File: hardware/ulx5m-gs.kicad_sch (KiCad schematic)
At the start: 4 parts

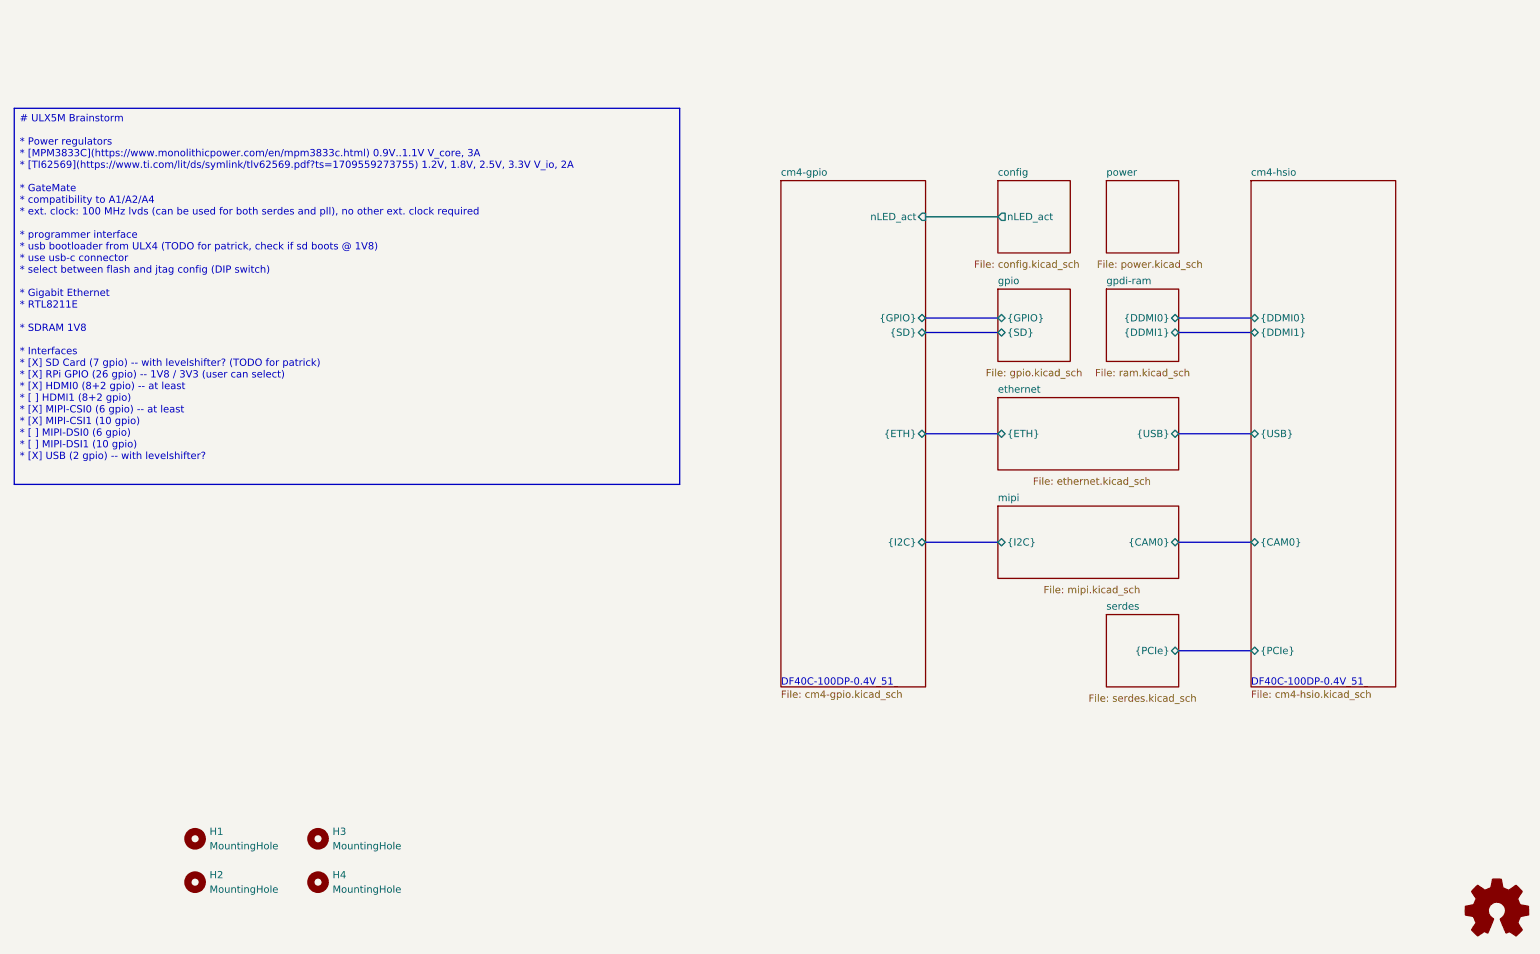
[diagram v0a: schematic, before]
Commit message: Adding USB connector and level converter
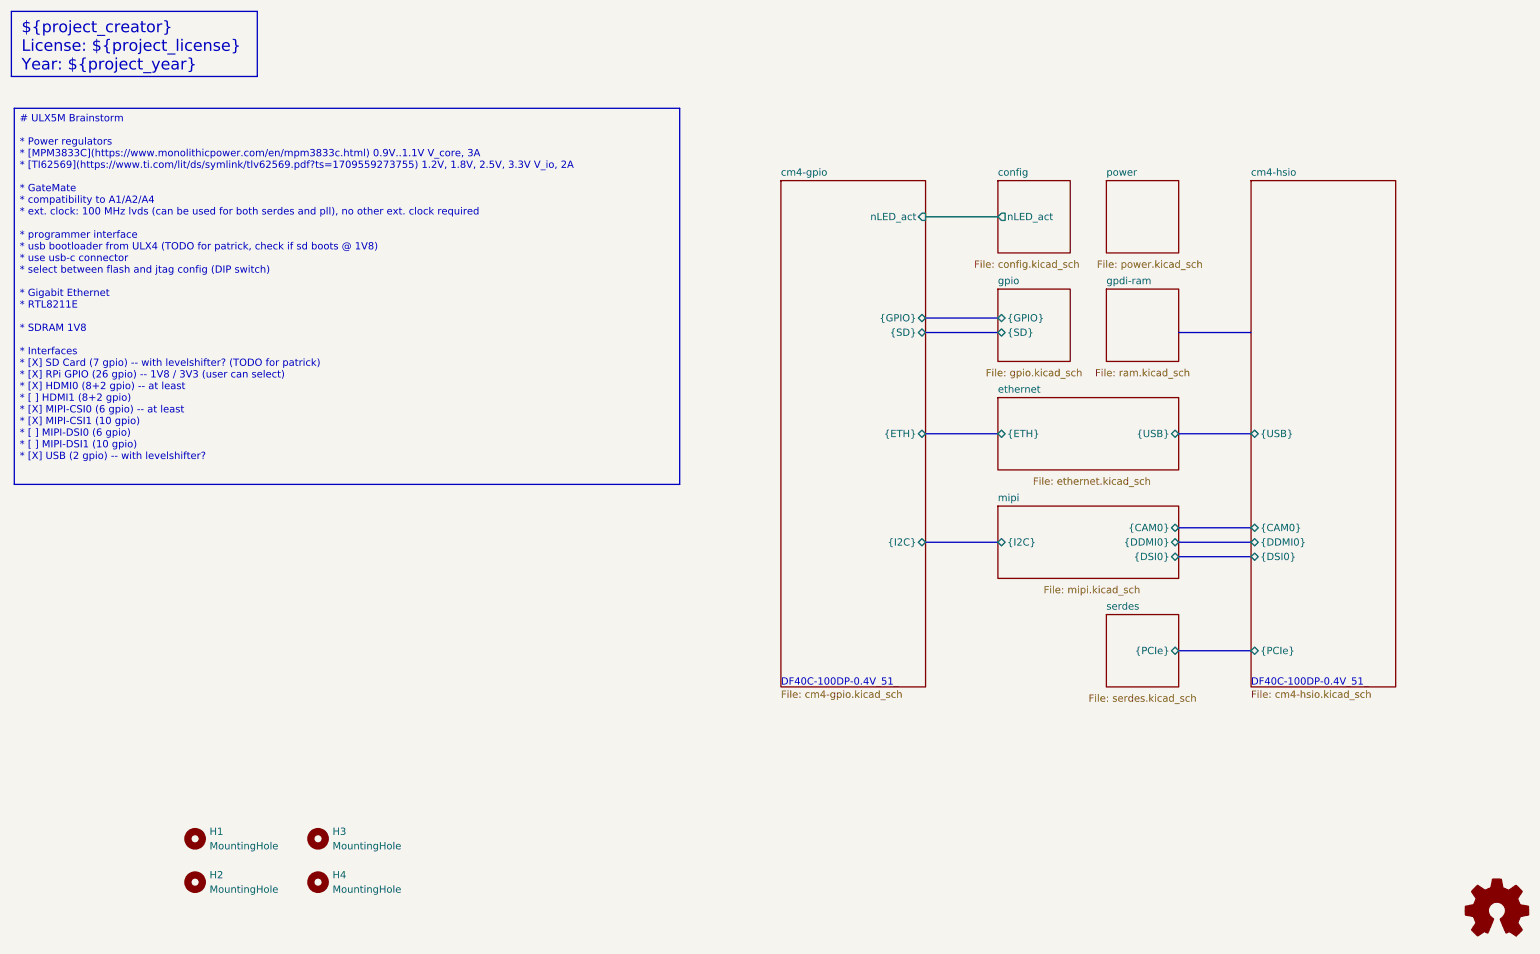
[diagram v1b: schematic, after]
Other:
- sheet cm4-hsio ports: added {DSI0}; removed {DDMI1}
- sheet gpdi-ram ports: added none; removed {DDMI0}, {DDMI1}
- sheet mipi ports: added {DDMI0}, {DSI0}; removed none
- note added: "${project_creator} License: ${project_license} Year: ${project_year}"
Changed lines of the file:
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@@
 		(date "2025-04-01")
+	)
+	(rectangle
+		(start 16.002 16.002)
+		(end 59.182 27.432)
+		(stroke
+			(width 0)
+			(type solid)
+		)
+		(fill
+			(type color)
+			(color 58 146 255 1)
+		)
 	)
 	(text "DF40C-100DP-0.4V_51_"
@@
 		)
 	)
+	(text "${project_creator}\nLicense: ${project_license}\nYear: ${project_year}"
+		(exclude_from_sim no)
+		(at 17.78 17.78 0)
+		(effects
+			(font
+				(size 2.032 2.032)
+			)
+			(justify left top)
+		)
+	)
 	(text_box "# ULX5M Brainstorm\n\n* Power regulators\n  * [MPM3833C](https://www.monolithicpower.com/en/mpm3833c.html) 0.9V..1.1V V_core, 3A\n  * [TI62569](https://www.ti.com/lit/ds/symlink/tlv62569.pdf?ts=1709559273755) 1.2V, 1.8V, 2.5V, 3.3V V_io, 2A\n\n* GateMate\n  * compatibility to A1/A2/A4\n  * ext. clock: 100 MHz lvds (can be used for both serdes and pll), no other ext. clock required\n\n* programmer interface\n  * usb bootloader from ULX4 (TODO for patrick, check if sd boots @ 1V8)\n  * use usb-c connector\n  * select between flash and jtag config (DIP switch)\n\n* Gigabit Ethernet\n  * RTL8211E\n\n* SDRAM 1V8\n\n* Interfaces\n  * [X] SD Card (7 gpio) -- with levelshifter? (TODO for patrick)\n  * [X] RPi GPIO (26 gpio) -- 1V8 / 3V3 (user can select)\n  * [X] HDMI0 (8+2 gpio) -- at least\n  * [ ] HDMI1 (8+2 gpio)\n  * [X] MIPI-CSI0 (6 gpio) -- at least\n  * [X] MIPI-CSI1 (10 gpio)\n  * [ ] MIPI-DSI0 (6 gpio)\n  * [ ] MIPI-DSI1 (10 gpio)\n  * [X] USB (2 gpio) -- with levelshifter?\n\n"
 		(exclude_from_sim no)
@@
 	(bus
 		(pts
-			(xy 220.98 69.85) (xy 233.68 69.85)
+			(xy 220.98 106.68) (xy 233.68 106.68)
 		)
 		(stroke
@@
 		(pts
 			(xy 176.53 69.85) (xy 189.23 69.85)
+		)
+		(stroke
+			(width 0)
+			(type default)
+		)
+	)
+	(bus
+		(pts
+			(xy 220.98 111.76) (xy 233.68 111.76)
 		)
 		(stroke
@@
 		)
 		(pin "{CAM0}" bidirectional
+			(at 220.98 106.68 0)
+			(effects
+				(font
+					(size 1.27 1.27)
+				)
+				(justify right)
+			)
+		)
+		(pin "{DDMI0}" bidirectional
 			(at 220.98 109.22 0)
+			(effects
+				(font
+					(size 1.27 1.27)
+				)
+				(justify right)
+			)
+		)
+		(pin "{DSI0}" bidirectional
+			(at 220.98 111.76 0)
 			(effects
 				(font
@@
 		)
 		(pin "{DDMI0}" bidirectional
-			(at 233.68 69.85 180)
+			(at 233.68 109.22 180)
 			(effects
 				(font
@@
 		)
 		(pin "{CAM0}" bidirectional
-			(at 233.68 109.22 180)
+			(at 233.68 106.68 180)
 			(effects
 				(font
@@
 			)
 		)
-		(pin "{DDMI1}" bidirectional
-			(at 233.68 72.39 180)
+		(pin "{DSI0}" bidirectional
+			(at 233.68 111.76 180)
 			(effects
 				(font
@@
 			)
 		)
-		(pin "{DDMI0}" bidirectional
-			(at 220.98 69.85 0)
-			(effects
-				(font
-					(size 1.27 1.27)
-				)
-				(justify right)
-			)
-		)
-		(pin "{DDMI1}" bidirectional
-			(at 220.98 72.39 0)
-			(effects
-				(font
-					(size 1.27 1.27)
-				)
-				(justify right)
-			)
-		)

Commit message: Routing diff clock
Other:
- company: (none) -> ${project_creator}
- title: (none) -> ${project_name}
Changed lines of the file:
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@@
 	(paper "A4")
 	(title_block
-		(date "2025-04-01")
+		(title "${project_name}")
+		(date "2025-06-24")
+		(rev "${project_version}")
+		(company "${project_creator}")
+		(comment 1 "${project_license}")
 	)
 	(rectangle

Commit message: Updat to CM5
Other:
- sheet cm4-gpio ports: added EEPROM_nWP, ETH_SYNC_O, FAN_PWM, FAN_TACHO, GPIO_VREF, ID_SC, ID_SD, LED_nPWR, PWR_BTN, USB_CC1, USB_CC2, VBAT, nRpiBOOT; removed none
- sheet cm4-hsio ports: added {DDMI1}, {MIPI0}, {MIPI1}, {USB3_0}; removed {CAM0}, {DSI0}
- sheet ethernet ports: added ID_SC, ID_SD, USB_CC1, USB_CC2, {DDMI1}, {I2C}; removed none
- sheet mipi ports: added {MIPI0}, {MIPI1}; removed {CAM0}, {DSI0}, {I2C}

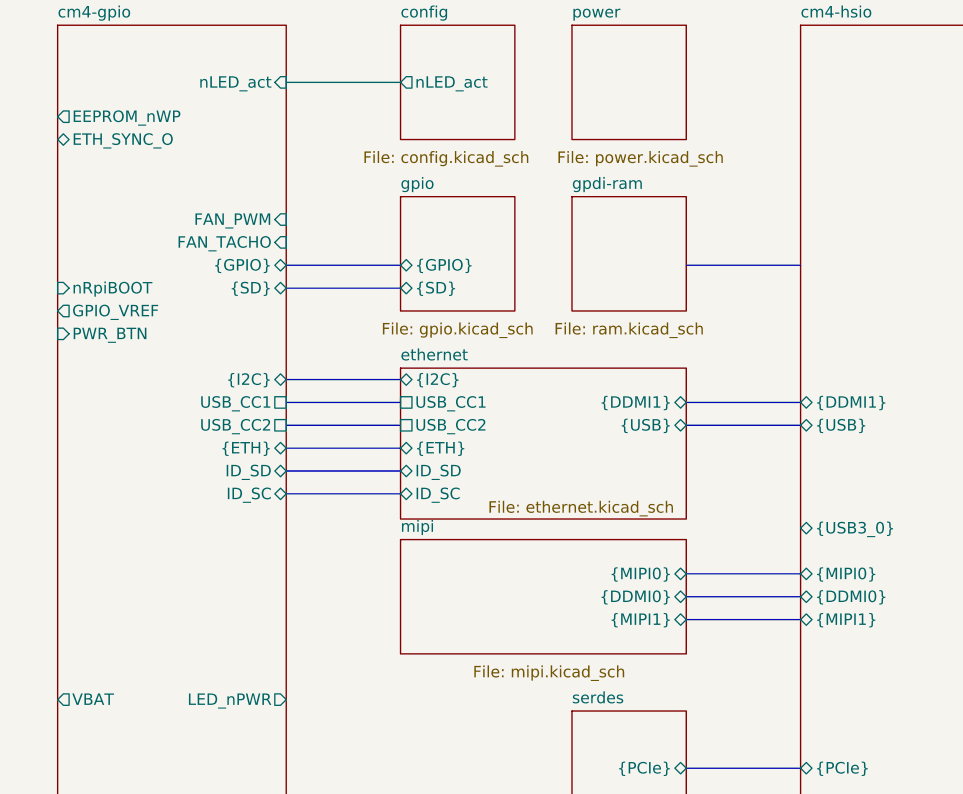
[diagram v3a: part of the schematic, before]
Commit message: Routing GPDI
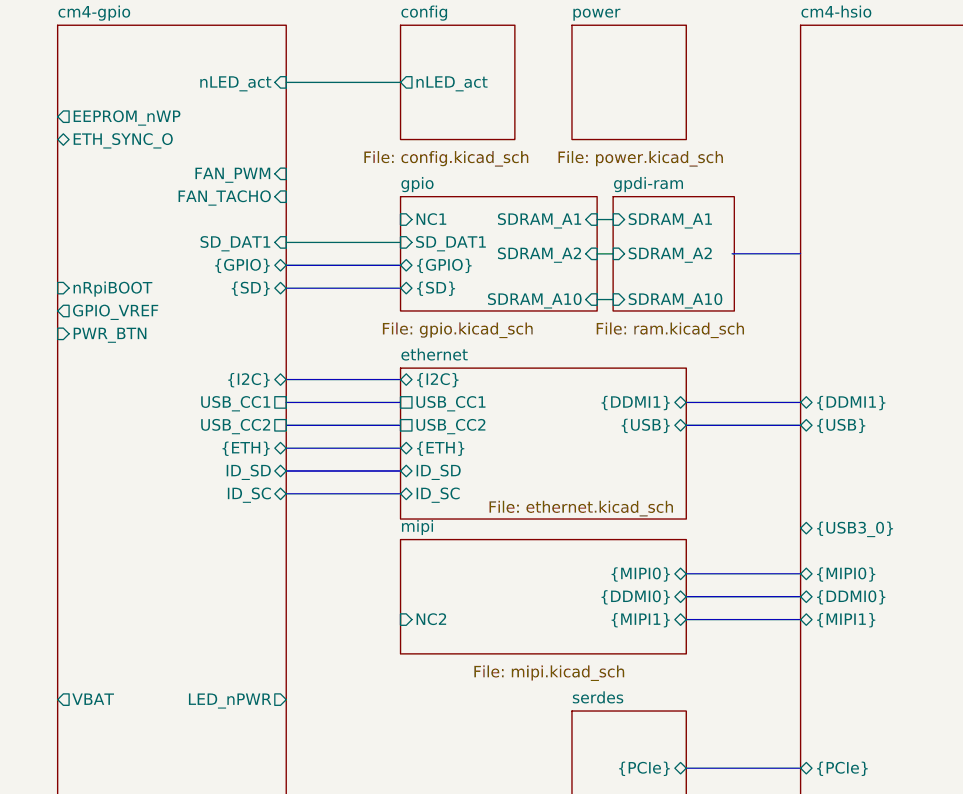
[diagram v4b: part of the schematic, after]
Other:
- sheet cm4-gpio ports: added SD_DAT1; removed none
- sheet gpdi-ram ports: added SDRAM_A1, SDRAM_A10, SDRAM_A2; removed none
- sheet gpio ports: added NC1, SDRAM_A1, SDRAM_A10, SDRAM_A2, SD_DAT1; removed none
- sheet mipi ports: added NC2; removed none
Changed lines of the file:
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@@
+		)
+	)
+	(wire
+		(pts
+			(xy 176.53 69.85) (xy 189.23 69.85)
+		)
+		(stroke
+			(width 0)
+			(type default)
 		)
 	)
@@
 		)
 	)
+	(wire
+		(pts
+			(xy 211.074 67.31) (xy 212.852 67.31)
+		)
+		(stroke
+			(width 0)
+			(type default)
+		)
+	)
 	(bus
 		(pts
@@
 		)
 	)
+	(wire
+		(pts
+			(xy 211.074 76.2) (xy 212.852 76.2)
+		)
+		(stroke
+			(width 0)
+			(type default)
+		)
+	)
 	(bus
 		(pts
@@
 		)
 	)
+	(wire
+		(pts
+			(xy 211.074 71.12) (xy 212.852 71.12)
+		)
+		(stroke
+			(width 0)
+			(type default)
+		)
+	)
 	(bus
 		(pts
@@
 		)
 	)
+	(bus
+		(pts
+			(xy 226.06 71.12) (xy 233.68 71.12)
+		)
+		(stroke
+			(width 0)
+			(type default)
+		)
+	)
 	(wire
 		(pts
 			(xy 176.53 52.07) (xy 189.23 52.07)
-		)
-		(stroke
-			(width 0)
-			(type default)
-		)
-	)
-	(bus
-		(pts
-			(xy 220.98 72.39) (xy 233.68 72.39)
 		)
 		(stroke
@@
 		)
 		(pin "FAN_PWM" input
-			(at 176.53 67.31 0)
+			(at 176.53 62.23 0)
 			(effects
 				(font
@@
 		)
 		(pin "FAN_TACHO" input
-			(at 176.53 69.85 0)
+			(at 176.53 64.77 0)
 			(effects
 				(font
@@
 				)
 				(justify left)
+			)
+		)
+		(pin "SD_DAT1" input
+			(at 176.53 69.85 0)
+			(effects
+				(font
+					(size 1.27 1.27)
+				)
+				(justify right)
 			)
 		)
@@
 	(sheet
 		(at 189.23 64.77)
-		(size 12.7 12.7)
+		(size 21.844 12.7)
 		(exclude_from_sim no)
 		(in_bom yes)
@@
 		(pin "{SD}" bidirectional
 			(at 189.23 74.93 180)
+			(effects
+				(font
+					(size 1.27 1.27)
+				)
+				(justify left)
+			)
+		)
+		(pin "SDRAM_A1" input
+			(at 211.074 67.31 0)
+			(effects
+				(font
+					(size 1.27 1.27)
+				)
+				(justify right)
+			)
+		)
+		(pin "SDRAM_A2" input
+			(at 211.074 71.12 0)
+			(effects
+				(font
+					(size 1.27 1.27)
+				)
+				(justify right)
+			)
+		)
+		(pin "SDRAM_A10" input
+			(at 211.074 76.2 0)
+			(effects
+				(font
+					(size 1.27 1.27)
+				)
+				(justify right)
+			)
+		)
+		(pin "SD_DAT1" input
+			(at 189.23 69.85 180)
+			(effects
+				(font
+					(size 1.27 1.27)
+				)
+				(justify left)
+			)
+		)
+		(pin "NC1" input
+			(at 189.23 67.31 180)
 			(effects
 				(font
@@
 			)
 		)
+		(pin "NC2" input
+			(at 189.23 111.76 180)
+			(effects
+				(font
+					(size 1.27 1.27)
+				)
+				(justify left)
+			)
+		)
 		(instances
 			(project "ulx5m-gs"
@@
 	)
 	(sheet
-		(at 208.28 64.77)
-		(size 12.7 12.7)
+		(at 212.852 64.77)
+		(size 13.462 12.7)
 		(exclude_from_sim no)
 		(in_bom yes)
@@
 		)
 		(property "Sheetname" "gpdi-ram"
-			(at 208.28 64.0584 0)
+			(at 212.852 64.0584 0)
 			(effects
 				(font
@@
 		)
 		(property "Sheetfile" "ram.kicad_sch"
-			(at 214.63 78.74 0)
+			(at 219.202 78.74 0)
 			(effects
 				(font
@@
 			)
 		)
+		(pin "SDRAM_A1" input
+			(at 212.852 67.31 180)
+			(effects
+				(font
+					(size 1.27 1.27)
+				)
+				(justify left)
+			)
+		)
+		(pin "SDRAM_A2" input
+			(at 212.852 71.12 180)
+			(effects
+				(font
+					(size 1.27 1.27)
+				)
+				(justify left)
+			)
+		)
+		(pin "SDRAM_A10" input
+			(at 212.852 76.2 180)
+			(effects
+				(font
+					(size 1.27 1.27)
+				)
+				(justify left)
+			)
+		)

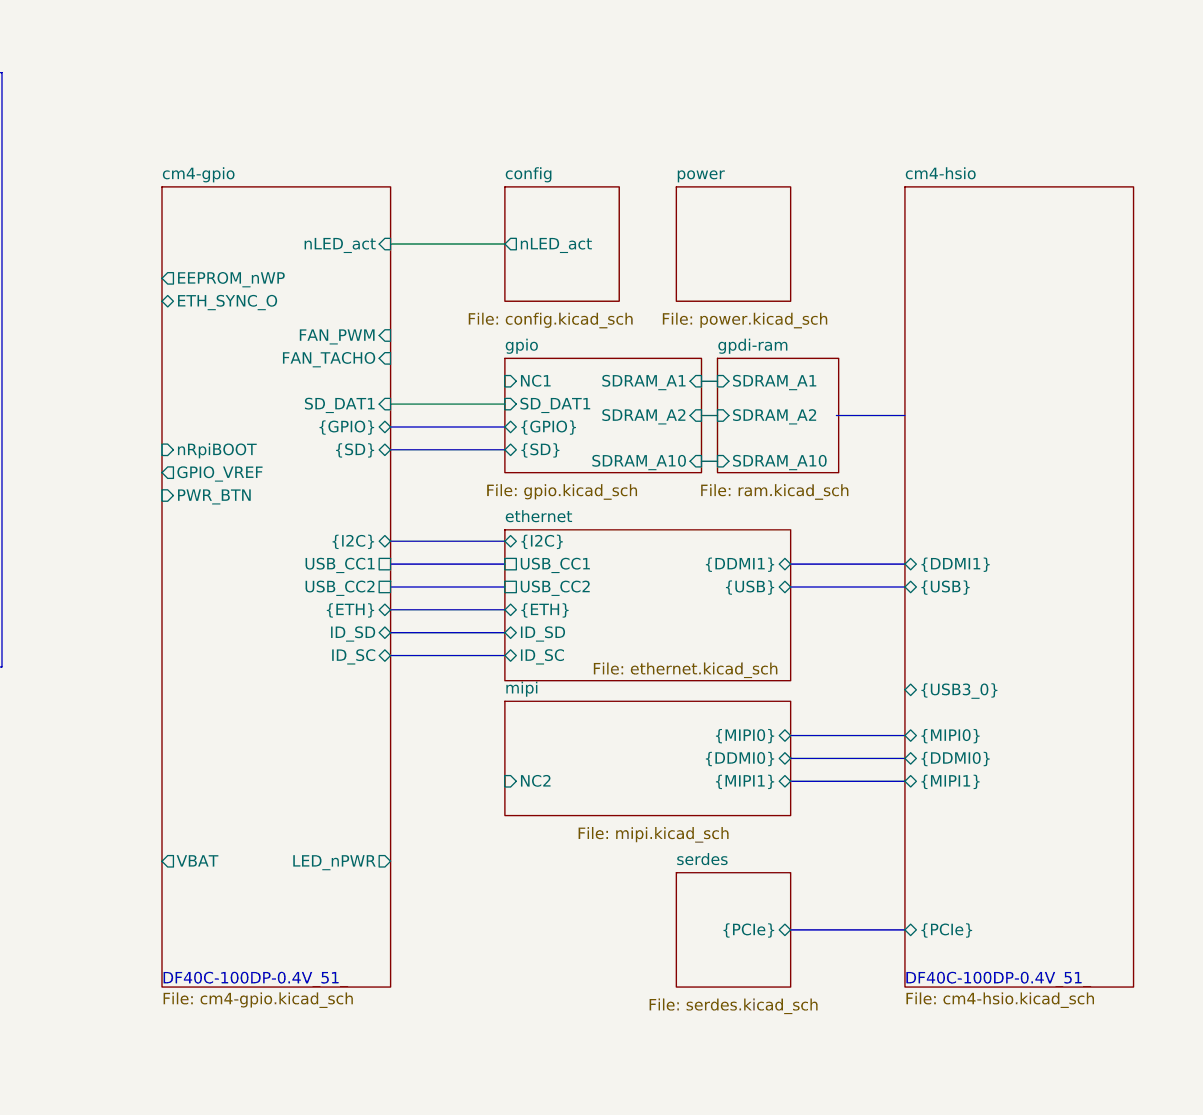
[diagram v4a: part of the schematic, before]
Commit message: Clearing ERC errors/warnings
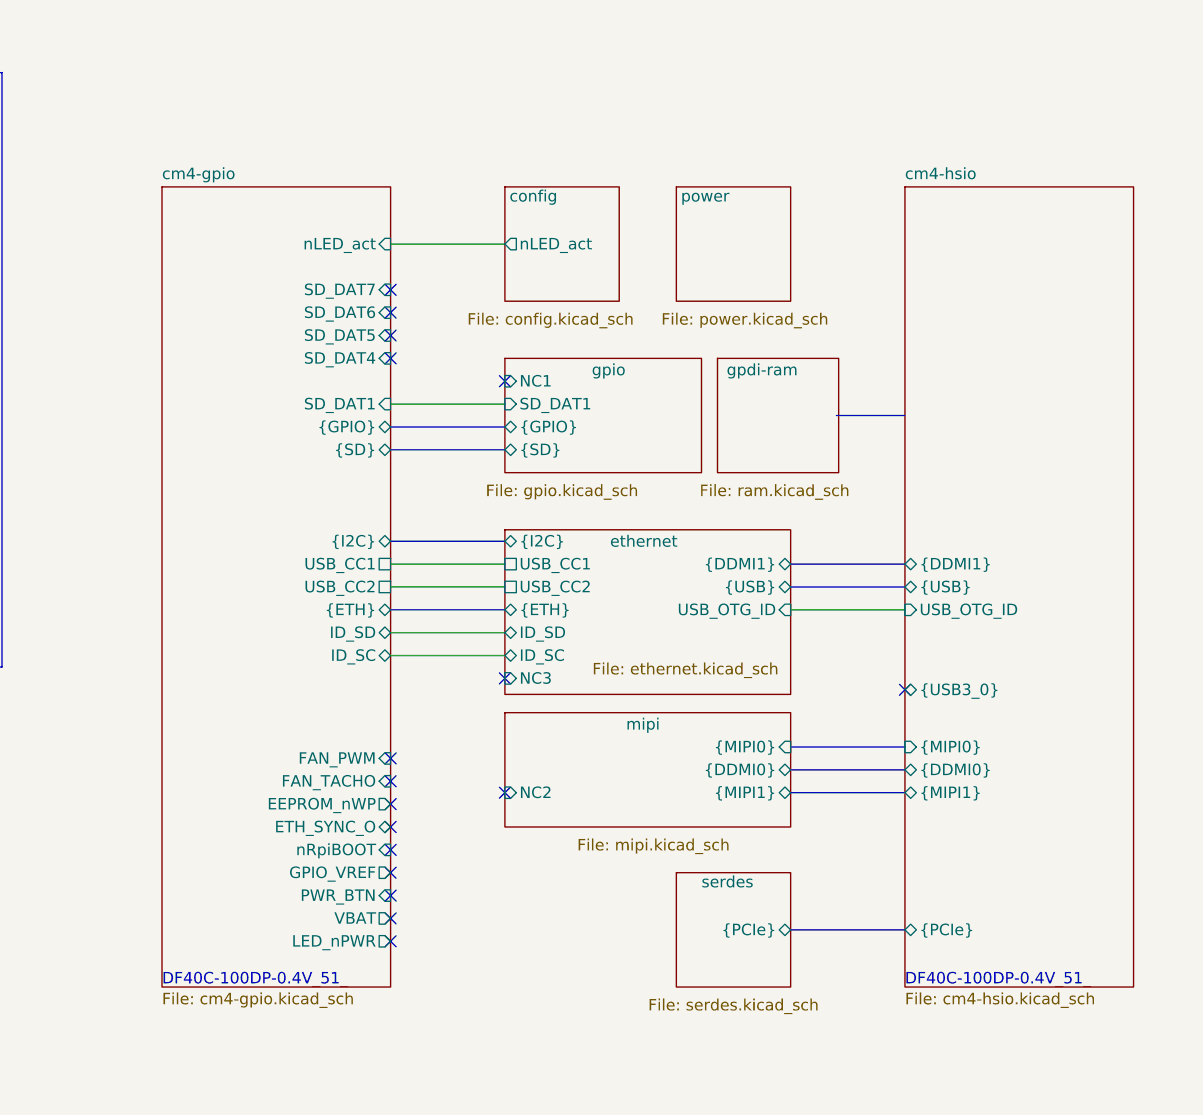
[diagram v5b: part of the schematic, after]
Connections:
- no-connect marks 0 -> 17
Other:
- sheet cm4-gpio ports: added SD_DAT4, SD_DAT5, SD_DAT6, SD_DAT7; removed none
- sheet cm4-hsio ports: added USB_OTG_ID; removed none
- sheet ethernet ports: added NC3, USB_OTG_ID; removed none
- sheet gpdi-ram ports: added none; removed SDRAM_A1, SDRAM_A10, SDRAM_A2
- sheet gpio ports: added none; removed SDRAM_A1, SDRAM_A10, SDRAM_A2
